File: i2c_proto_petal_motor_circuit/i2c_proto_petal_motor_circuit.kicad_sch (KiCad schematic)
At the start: 17 parts, among them J1 From Badge, M1 Vibro Motor, M2 Solenoid, M3 Buzzer Motor, Q1 2N2222 (NPN), Q2 2N2222 (NPN), Q3 2N2222 (NPN), SW1 SW_Push, U1 CH32V003F4P6

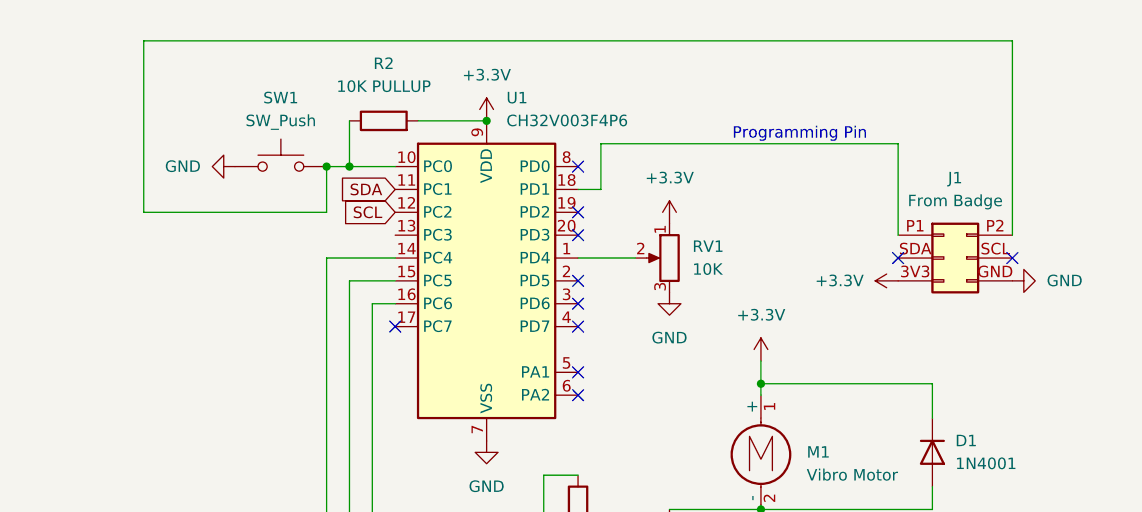
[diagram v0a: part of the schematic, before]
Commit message: updated schematic with 2 x LEDs
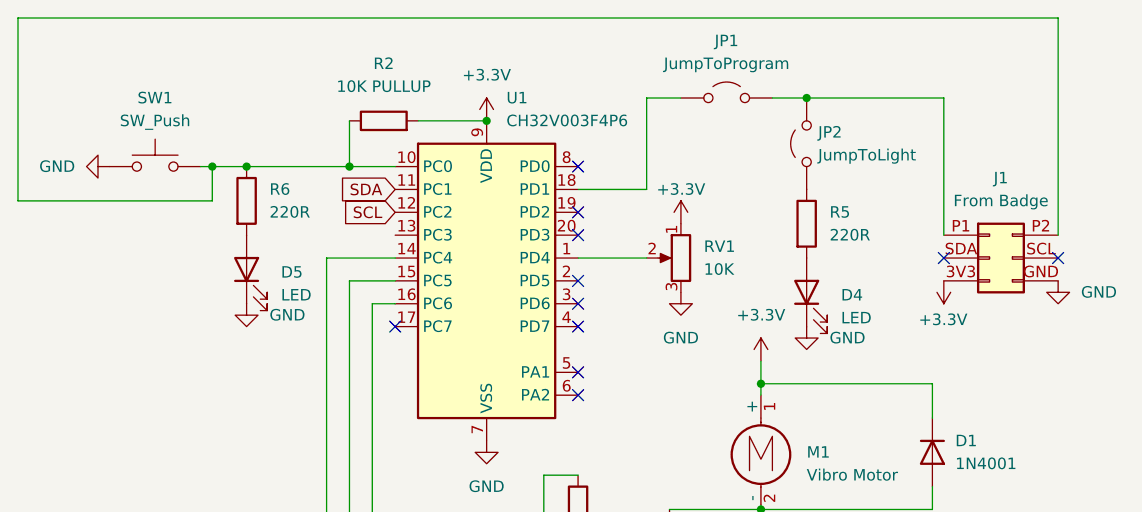
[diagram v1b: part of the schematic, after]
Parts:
- added D4, D5: LED, symbol Device:LED
- added JP1: JumpToProgram, symbol Jumper:Jumper_2_Open
- added JP2: JumpToLight, symbol Jumper:Jumper_2_Open
- added R5, R6: 220R, symbol Device:R
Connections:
- net GND: now also D4.1 (K), D5.1 (K)
- net at J1.P2 (+12V), R2.1, SW1.2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: now also R6.1
- net at J1.P1 (+12V): now also JP1.2 (B), JP2.2 (B); no longer U1.18 (PD1)
- new net: JP2.1 (A), R5.1
- new net: D4.2 (A), R5.2
- new net: D5.2 (A), R6.2
- new net: JP1.1 (A), U1.18 (PD1)
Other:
- note removed: "Programming Pin"
- moved on the sheet: J1, RV1, SW1

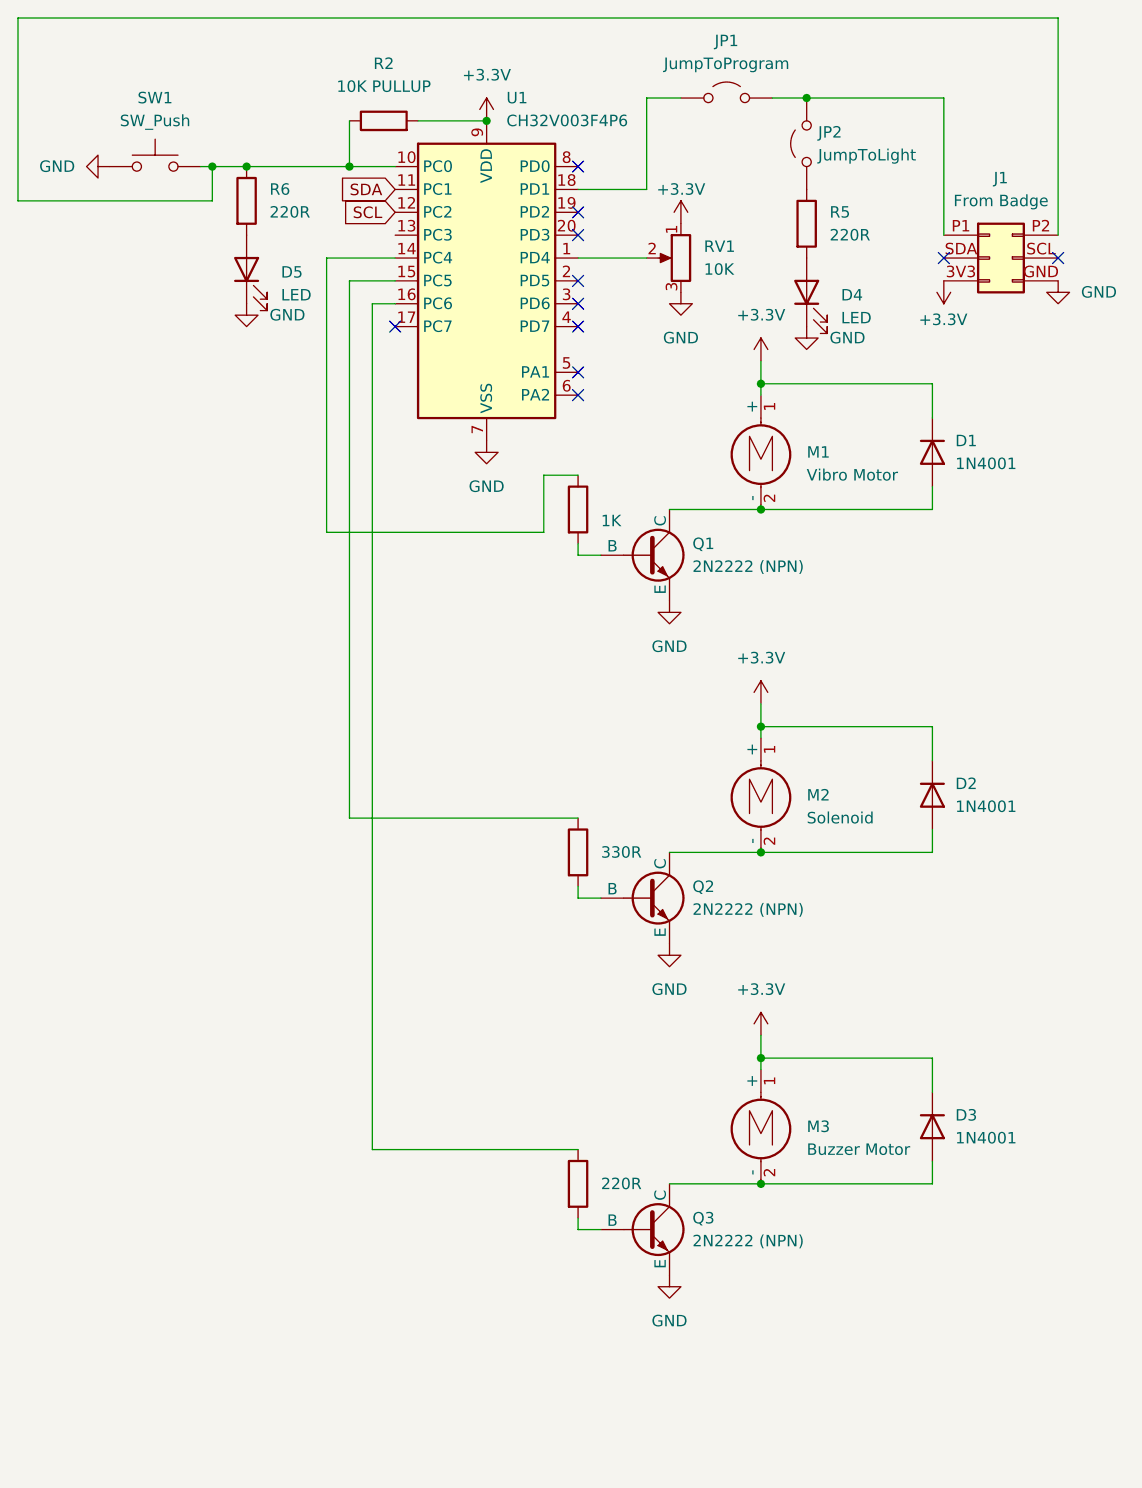
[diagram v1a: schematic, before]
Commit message: made new schematic for proto petal
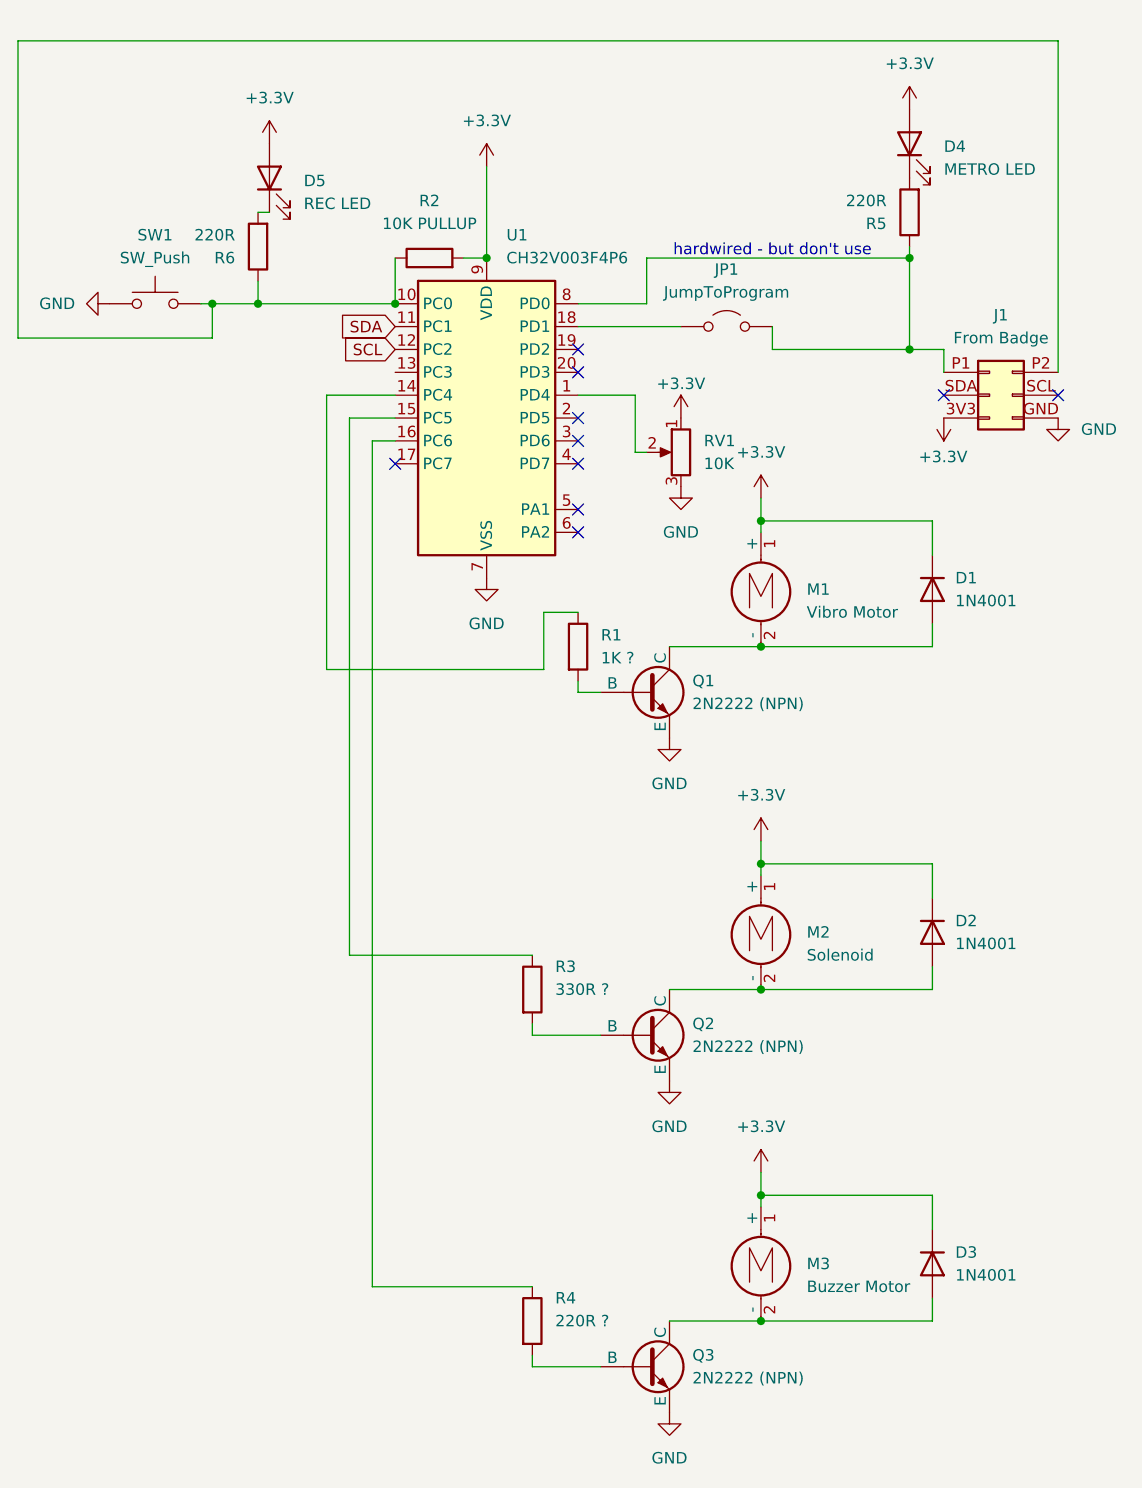
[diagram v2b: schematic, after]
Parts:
- removed JP2: JumpToLight, symbol Jumper:Jumper_2_Open
- D4: value LED -> METRO LED
- D5: value LED -> REC LED
- R1: value 1K -> 1K ?
- R3: value 330R -> 330R ?
- R4: value 220R -> 220R ?
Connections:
- net +3.3V: now also D4.2 (A), D5.2 (A)
- net GND: no longer D4.1 (K), D5.1 (K)
- net at R5.1: now also J1.P1 (+12V), JP1.2 (B), U1.8 (PD0)
- net at R5.2: now also D4.1 (K); no longer D4.2 (A)
- net at R6.2: now also D5.1 (K); no longer D5.2 (A)
- no-connect marks 11 -> 10
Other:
- note added: "hardwired - but don't use"
- moved on the sheet: D1, D2, D3, J1, JP1, M1, M2, M3, Q1, Q2, Q3, R2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
